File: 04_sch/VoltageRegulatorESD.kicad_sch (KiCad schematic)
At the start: 27 parts, among them Q1 IRF5305S, SW3 SW_SPDT_321, U2 MP1584EN, U3 AMS1117

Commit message: Fix tantalum capacitor & JLCPCB codes
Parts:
- C10, C14, C6, C8: LCSC (none) -> C49678
- C11: LCSC (none) -> C1790
- C12, C13, C7, C9: LCSC (none) -> C15850
- D3: LCSC C3039962 -> C8678
- D5: LCSC (none) -> C19171391
- L1: LCSC (none) -> C108295
- R10: LCSC (none) -> C17513
- R11, R12, R7, R8, R9: LCSC (none) -> C149504
- R13: LCSC (none) -> C17828
- R14: LCSC (none) -> C966144
- RV1: LCSC (none) -> C128551
- U3: LCSC (none) -> C917183
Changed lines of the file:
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@@
 			)
 		)
-		(property "LCSC" ""
+		(property "LCSC" "C149504"
 			(at 143.51 67.31 0)
 			(effects
@@
 			)
 		)
-		(property "LCSC" ""
+		(property "LCSC" "C1790"
 			(at 190.5 76.2 0)
 			(effects
@@
 			)
 		)
-		(property "LCSC" ""
+		(property "LCSC" "C966144"
 			(at 99.06 130.81 0)
 			(effects
@@
 			)
 		)
-		(property "LCSC" ""
+		(property "LCSC" "C15850"
 			(at 224.79 67.31 0)
 			(effects
@@
 			)
 		)
-		(property "LCSC" ""
+		(property "LCSC" "C15850"
 			(at 60.96 134.62 0)
 			(effects
@@
 			)
 		)
-		(property "LCSC" ""
+		(property "LCSC" "C17828"
 			(at 204.47 81.28 0)
 			(effects
@@
 			)
 		)
-		(property "LCSC" ""
+		(property "LCSC" "C49678"
 			(at 92.71 134.62 0)
 			(effects
@@
 			)
 		)
-		(property "LCSC" ""
+		(property "LCSC" "C149504"
 			(at 194.31 81.28 0)
 			(effects
@@
 			)
 		)
-		(property "LCSC" ""
+		(property "LCSC" "C108295"
 			(at 208.28 64.77 0)
 			(effects
@@
 			)
 		)
-		(property "LCSC" ""
+		(property "LCSC" "C149504"
 			(at 83.82 76.2 0)
 			(effects
@@
 			)
 		)
-		(property "LCSC" ""
+		(property "LCSC" "C17513"
 			(at 100.33 76.2 0)
 			(effects
@@
 			)
 		)
-		(property "LCSC" ""
+		(property "LCSC" "C49678"
 			(at 138.43 69.85 0)
 			(effects
@@
 			)
 		)
-		(property "LCSC" ""
+		(property "LCSC" "C149504"
 			(at 143.51 72.39 0)
 			(effects
@@
 			)
 		)
-		(property "LCSC" ""
+		(property "LCSC" "C15850"
 			(at 129.54 69.85 0)
 			(effects
@@
 			)
 		)
-		(property "LCSC" ""
+		(property "LCSC" "C917183"
 			(at 71.12 130.81 0)
 			(effects
@@
 			)
 		)
-		(property "LCSC" ""
+		(property "LCSC" "C15850"
 			(at 85.09 134.62 0)
 			(effects
@@
 			)
 		)
-		(property "LCSC" ""
+		(property "LCSC" "C149504"
 			(at 148.59 77.47 0)
 			(effects
@@
 			)
 		)
-		(property "LCSC" ""
+		(property "LCSC" "C128551"
 			(at 215.9 68.58 0)
 			(effects
@@
 			)
 		)
-		(property "LCSC" ""
+		(property "LCSC" "C49678"
 			(at 184.15 62.23 0)
 			(effects
@@
 			)
 		)
-		(property "LCSC" ""
+		(property "LCSC" "C49678"
 			(at 232.41 67.31 0)
 			(effects
@@
 			)
 		)
-		(property "LCSC" "C3039962"
+		(property "LCSC" "C8678"
 			(at 195.58 59.69 0)
 			(effects
@@
 			)
 		)
-		(property "LCSC" ""
+		(property "LCSC" "C19171391"
 			(at 107.95 130.81 0)
 			(effects

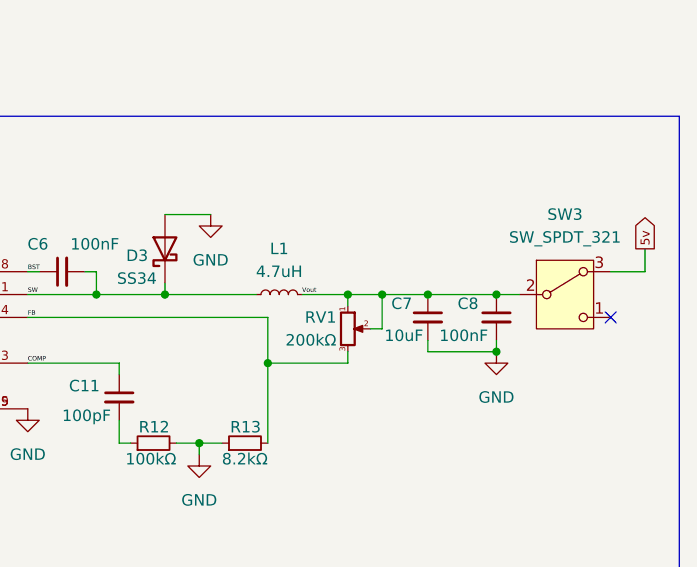
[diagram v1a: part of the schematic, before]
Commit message: Testpoint to Vout
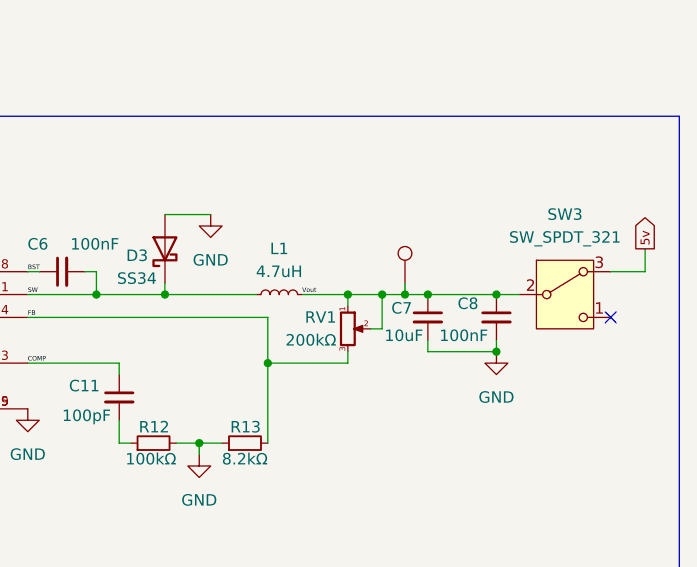
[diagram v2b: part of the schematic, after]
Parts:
- added TP1: TestPoint, TestPoint:TestPoint_Pad_D1.0mm, symbol Connector:TestPoint
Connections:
- net Vout: now also TP1.1
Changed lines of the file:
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@@
 	)
 	(junction
+		(at 222.25 64.77)
+		(diameter 0)
+		(color 0 0 0 0)
+	)
+	(junction
 		(at 232.41 64.77)
 		(diameter 0)
@@
 	(wire
 		(pts
+			(xy 222.25 64.77) (xy 224.79 64.77)
+		)
+		(stroke
+			(width 0)
+			(type default)
+		)
+	)
+	(wire
+		(pts
 			(xy 187.96 62.23) (xy 187.96 64.77)
 		)
@@
 	(wire
 		(pts
+			(xy 222.25 63.5) (xy 222.25 64.77)
+		)
+		(stroke
+			(width 0)
+			(type default)
+		)
+	)
+	(wire
+		(pts
 			(xy 60.96 138.43) (xy 60.96 137.16)
 		)
@@
 	(wire
 		(pts
-			(xy 219.71 64.77) (xy 224.79 64.77)
+			(xy 219.71 64.77) (xy 222.25 64.77)
 		)
 		(stroke
@@
 		(dnp no)
 		(property "Reference" "C7"
-			(at 220.726 65.786 0)
+			(at 220.726 66.294 0)
 			(effects
 				(font
@@
 					(unit 1)
 				)
+			)
+		)
+	)
+	(symbol
+		(lib_id "Connector:TestPoint")
+		(at 222.25 63.5 0)
+		(unit 1)
+		(exclude_from_sim yes)
+		(in_bom no)
+		(on_board yes)
+		(dnp no)
+		(fields_autoplaced yes)
+		(property "Reference" "TP1"
+			(at 224.79 58.9279 0)
+			(effects
+				(font
+					(size 1.27 1.27)
+				)
+				(justify left)
+				(hide yes)
+			)
+		)
+		(property "Value" "TestPoint"
+			(at 224.79 61.4679 0)
+			(effects
+				(font
+					(size 1.27 1.27)
+				)
+				(justify left)
+				(hide yes)
+			)
+		)
+		(property "Footprint" "TestPoint:TestPoint_Pad_D1.0mm"
+			(at 227.33 63.5 0)
+			(effects
+				(font
+					(size 1.27 1.27)
+				)
+				(hide yes)
+			)
+		)
+		(property "Datasheet" "~"
+			(at 227.33 63.5 0)
+			(effects
+				(font
+					(size 1.27 1.27)
+				)
+				(hide yes)
+			)
+		)
+		(property "Description" "test point"
+			(at 222.25 63.5 0)
+			(effects
+				(font
+					(size 1.27 1.27)
+				)
+				(hide yes)
+			)
+		)
+		(pin "1"
+		)
+		(instances
+			(project ""
+				(path "/4ec2d2e6-55cd-4bab-92e3-628cee37171a/6d3e4366-3421-462a-9b2c-4d2da3cc968c"
+					(reference "TP1")
+					(unit 1)
+				)
